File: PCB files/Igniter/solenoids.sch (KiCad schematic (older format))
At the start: 28 parts, among them Q2 N MOSFET, Q3 N MOSFET, Q4 N MOSFET, Q5 N MOSFET, Q6 N MOSFET, U2 FDS8984, U3 FDS8984, U4 FDS8984

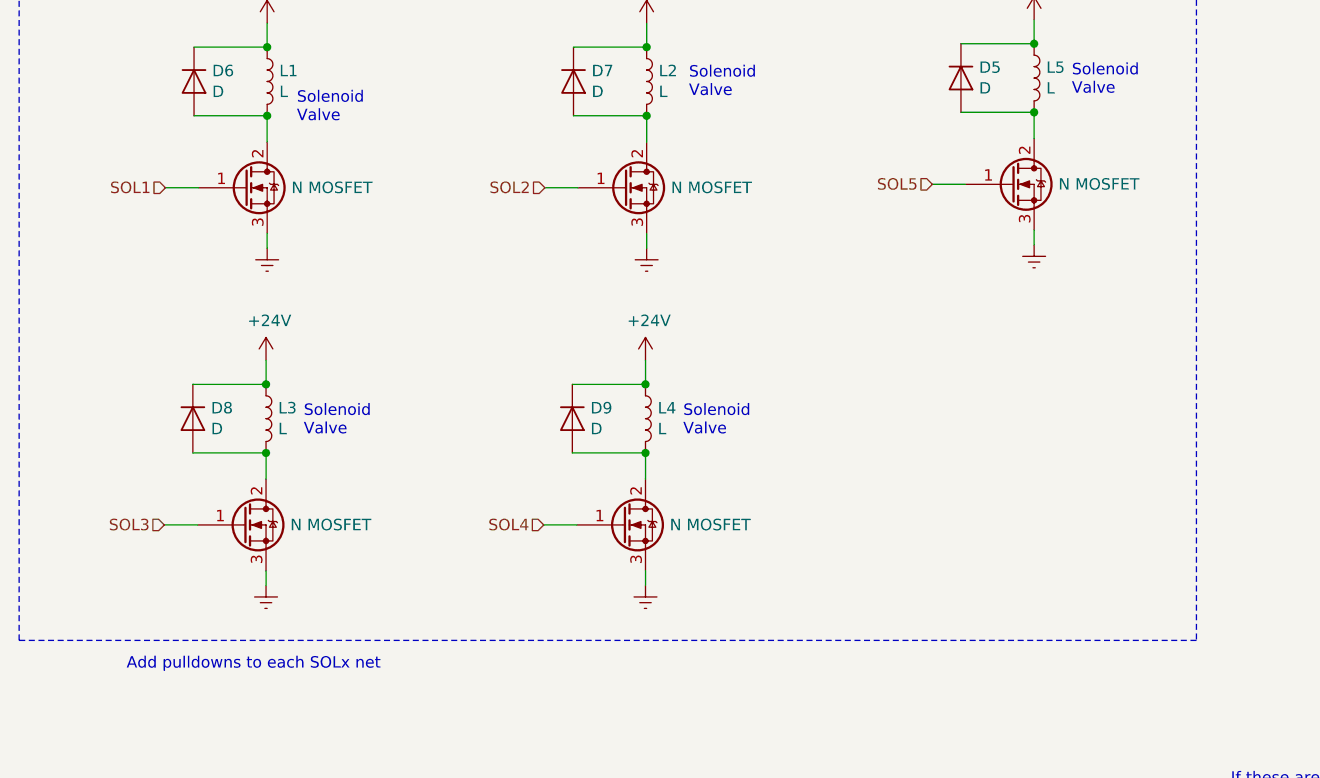
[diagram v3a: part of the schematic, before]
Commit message: 11/16/2019
-Selected smaller MOSFET SOT223
-Condensed PCB to a much smaller size
-Added Solenoid pulldowns
-Added all momentary switches
-Shrunk all resistors to 1206
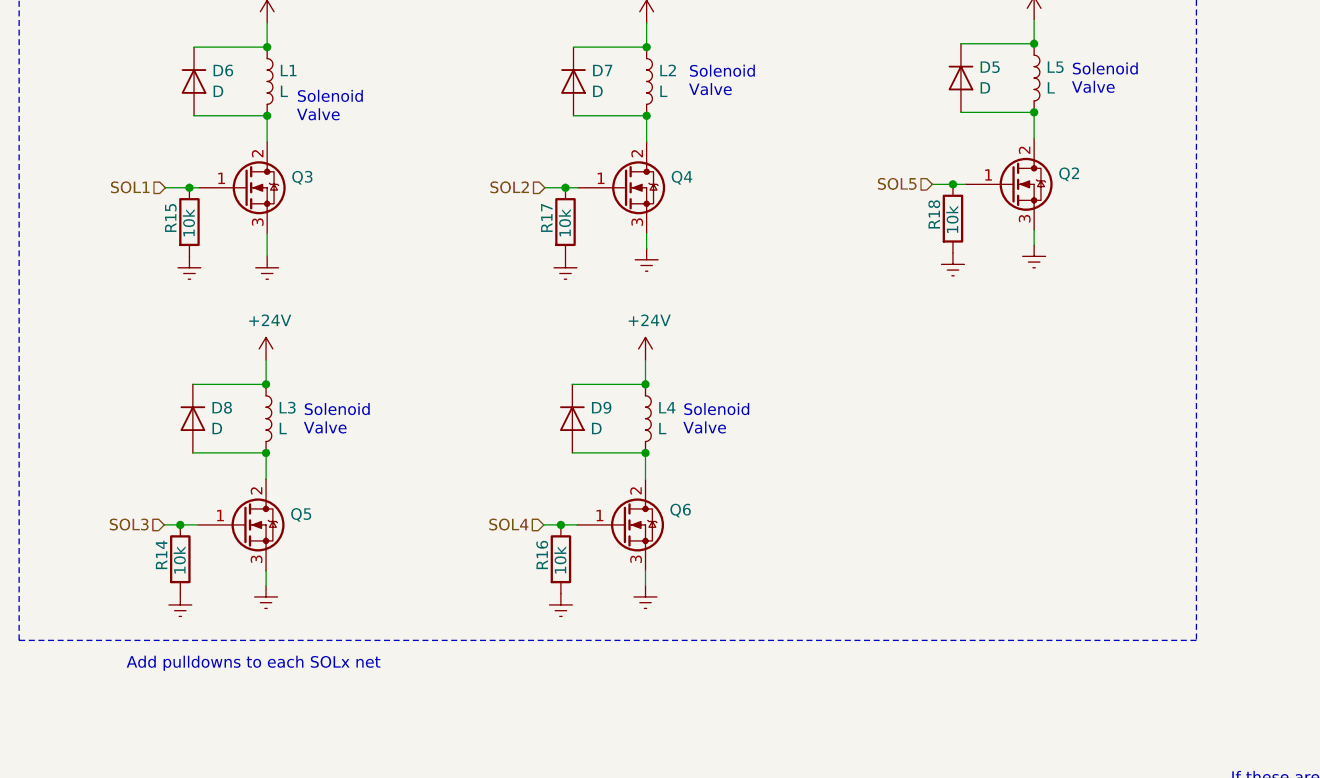
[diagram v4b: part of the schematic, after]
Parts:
- added R14, R15, R16, R17, R18: 10k, Resistor_SMD:R_1206_3216Metric, symbol Device:R
- Q2, Q3, Q4, Q5, Q6: footprint Package_TO_SOT_SMD:TO-263-3_TabPin2 -> Package_TO_SOT_SMD:SOT-223
- R10, R5, R7, R8, R9: footprint Resistor_SMD:R_1210_3225Metric -> Resistor_SMD:R_1206_3216Metric
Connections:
- net GNDREF: now also R14.2, R15.2, R16.2, R17.2, R18.2
- net SOL1: now also R15.1
- net SOL2: now also R17.1
- net SOL3: now also R14.1
- net SOL4: now also R16.1
- net SOL5: now also R18.1
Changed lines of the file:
@@
 	1830 2635 2150 2635
 Connection ~ 2150 2335
-Wire Wire Line
-	1705 2950 1850 2950
 Text Notes 2280 2670 0    50   ~ 0
 Solenoid\nValve
@@
 L power:GNDREF #PWR029
 U 1 1 5DB4DF2B
-P 2150 3215
-F 0 "#PWR029" H 2150 2965 50  0001 C CNN
-F 1 "GNDREF" H 2155 3042 50  0001 C CNN
-F 2 "" H 2150 3215 50  0001 C CNN
-F 3 "" H 2150 3215 50  0001 C CNN
-	1    2150 3215
-	1    0    0    -1
-$EndComp
-Wire Wire Line
-	2150 3150 2150 3215
+P 2150 3250
+F 0 "#PWR029" H 2150 3000 50  0001 C CNN
+F 1 "GNDREF" H 2155 3077 50  0001 C CNN
+F 2 "" H 2150 3250 50  0001 C CNN
+F 3 "" H 2150 3250 50  0001 C CNN
+	1    2150 3250
+	1    0    0    -1
+$EndComp
+Wire Wire Line
+	2150 3150 2150 3250
 $Comp
 L Device:Q_NMOS_GDS Q?
@@
 AR Path="/5DB4DFB4" Ref="Q?"  Part="1"
 AR Path="/5DB4D508/5DB4DFB4" Ref="Q3"  Part="1"
-F 0 "Q3" H 2256 2996 50  0001 L CNN
-F 1 "N MOSFET" H 2256 2950 50  0000 L CNN
-F 2 "Package_TO_SOT_SMD:TO-263-3_TabPin2" H 2250 3050 50  0001 C CNN
+F 0 "Q3" H 2256 2996 50  0000 L CNN
+F 1 "N MOSFET" H 2256 2950 50  0001 L CNN
+F 2 "Package_TO_SOT_SMD:SOT-223" H 2250 3050 50  0001 C CNN
 F 3 "~" H 2050 2950 50  0001 C CNN
 	1    2050 2950
@@
 AR Path="/5DB4DFC6" Ref="Q?"  Part="1"
 AR Path="/5DB4D508/5DB4DFC6" Ref="Q5"  Part="1"
-F 0 "Q5" H 2251 4471 50  0001 L CNN
-F 1 "N MOSFET" H 2251 4425 50  0000 L CNN
-F 2 "Package_TO_SOT_SMD:TO-263-3_TabPin2" H 2245 4525 50  0001 C CNN
+F 0 "Q5" H 2251 4471 50  0000 L CNN
+F 1 "N MOSFET" H 2251 4425 50  0001 L CNN
+F 2 "Package_TO_SOT_SMD:SOT-223" H 2245 4525 50  0001 C CNN
 F 3 "~" H 2045 4425 50  0001 C CNN
 	1    2045 4425
@@
 AR Path="/5DB4DFC0" Ref="Q?"  Part="1"
 AR Path="/5DB4D508/5DB4DFC0" Ref="Q6"  Part="1"
-F 0 "Q6" H 3911 4471 50  0001 L CNN
-F 1 "N MOSFET" H 3911 4425 50  0000 L CNN
-F 2 "Package_TO_SOT_SMD:TO-263-3_TabPin2" H 3905 4525 50  0001 C CNN
+F 0 "Q6" H 3910 4490 50  0000 L CNN
+F 1 "N MOSFET" H 3911 4425 50  0001 L CNN
+F 2 "Package_TO_SOT_SMD:SOT-223" H 3905 4525 50  0001 C CNN
 F 3 "~" H 3705 4425 50  0001 C CNN
 	1    3705 4425
@@
 Solenoid\nValve
 Wire Wire Line
-	3360 4425 3505 4425
+	3360 4425 3435 4425
 Wire Wire Line
 	3485 4110 3805 4110
@@
 Solenoid\nValve
 Wire Wire Line
-	1700 4425 1845 4425
+	1700 4425 1770 4425
 Wire Wire Line
 	1825 4110 2145 4110
@@
 AR Path="/5DB4DFF7" Ref="Q?"  Part="1"
 AR Path="/5DB4D508/5DB4DFF7" Ref="Q2"  Part="1"
-F 0 "Q2" H 5611 2981 50  0001 L CNN
-F 1 "N MOSFET" H 5611 2935 50  0000 L CNN
-F 2 "Package_TO_SOT_SMD:TO-263-3_TabPin2" H 5605 3035 50  0001 C CNN
+F 0 "Q2" H 5611 2981 50  0000 L CNN
+F 1 "N MOSFET" H 5611 2935 50  0001 L CNN
+F 2 "Package_TO_SOT_SMD:SOT-223" H 5605 3035 50  0001 C CNN
 F 3 "~" H 5405 2935 50  0001 C CNN
 	1    5405 2935
@@
 Solenoid\nValve
 Wire Wire Line
-	5060 2935 5205 2935
+	5060 2935 5150 2935
 Wire Wire Line
 	5185 2620 5505 2620
@@
 AR Path="/5DB4DFBA" Ref="Q?"  Part="1"
 AR Path="/5DB4D508/5DB4DFBA" Ref="Q4"  Part="1"
-F 0 "Q4" H 3916 2996 50  0001 L CNN
-F 1 "N MOSFET" H 3916 2950 50  0000 L CNN
-F 2 "Package_TO_SOT_SMD:TO-263-3_TabPin2" H 3910 3050 50  0001 C CNN
+F 0 "Q4" H 3916 2996 50  0000 L CNN
+F 1 "N MOSFET" H 3916 2950 50  0001 L CNN
+F 2 "Package_TO_SOT_SMD:SOT-223" H 3910 3050 50  0001 C CNN
 F 3 "~" H 3710 2950 50  0001 C CNN
 	1    3710 2950
@@
 	3810 2230 3810 2335
 Wire Wire Line
-	3365 2950 3510 2950
+	3365 2950 3455 2950
 Wire Wire Line
 	3490 2635 3810 2635
@@
 F 0 "R5" V 7155 2890 50  0000 C CNN
 F 1 "1k2" V 7235 2890 50  0000 C CNN
-F 2 "Resistor_SMD:R_1210_3225Metric" V 7165 2890 50  0001 C CNN
+F 2 "Resistor_SMD:R_1206_3216Metric" V 7165 2890 50  0001 C CNN
 F 3 "~" H 7235 2890 50  0001 C CNN
 	1    7235 2890
@@
 F 0 "R8" V 7390 3090 50  0000 C CNN
 F 1 "1k2" V 7475 3090 50  0000 C CNN
-F 2 "Resistor_SMD:R_1210_3225Metric" V 7405 3090 50  0001 C CNN
+F 2 "Resistor_SMD:R_1206_3216Metric" V 7405 3090 50  0001 C CNN
 F 3 "~" H 7475 3090 50  0001 C CNN
 	1    7475 3090
@@
 F 0 "R10" V 8885 3110 50  0000 C CNN
 F 1 "1k2" V 8965 3110 50  0000 C CNN
-F 2 "Resistor_SMD:R_1210_3225Metric" V 8895 3110 50  0001 C CNN
+F 2 "Resistor_SMD:R_1206_3216Metric" V 8895 3110 50  0001 C CNN
 F 3 "~" H 8965 3110 50  0001 C CNN
 	1    8965 3110
@@
 F 0 "R7" V 7155 3760 50  0000 C CNN
 F 1 "1k2" V 7235 3760 50  0000 C CNN
-F 2 "Resistor_SMD:R_1210_3225Metric" V 7165 3760 50  0001 C CNN
+F 2 "Resistor_SMD:R_1206_3216Metric" V 7165 3760 50  0001 C CNN
 F 3 "~" H 7235 3760 50  0001 C CNN
 	1    7235 3760
@@
 F 0 "R9" V 7395 3960 50  0000 C CNN
 F 1 "1k2" V 7475 3960 50  0000 C CNN
-F 2 "Resistor_SMD:R_1210_3225Metric" V 7405 3960 50  0001 C CNN
+F 2 "Resistor_SMD:R_1206_3216Metric" V 7405 3960 50  0001 C CNN
 F 3 "~" H 7475 3960 50  0001 C CNN
 	1    7475 3960
@@
 Text Notes 1535 5065 0    50   ~ 0
 Add pulldowns to each SOLx net
+$Comp
+L Device:R R?
+U 1 1 5DD0DFB3
+P 1810 3100
+AR Path="/5DD0DFB3" Ref="R?"  Part="1"
+AR Path="/5DB4D508/5DD0DFB3" Ref="R15"  Part="1"
+F 0 "R15" V 1730 3050 50  0000 L CNN
+F 1 "10k" V 1810 3030 50  0000 L CNN
+F 2 "Resistor_SMD:R_1206_3216Metric" V 1740 3100 50  0001 C CNN
+F 3 "~" H 1810 3100 50  0001 C CNN
+	1    1810 3100
+	1    0    0    -1
+$EndComp
+$Comp
+L power:GNDREF #PWR?
+U 1 1 5DD0DFBA
+P 1810 3250
+AR Path="/5DD0DFBA" Ref="#PWR?"  Part="1"
+AR Path="/5DB4D508/5DD0DFBA" Ref="#PWR050"  Part="1"
+F 0 "#PWR050" H 1810 3000 50  0001 C CNN
+F 1 "GNDREF" H 1815 3077 50  0001 C CNN
+F 2 "" H 1810 3250 50  0001 C CNN
+F 3 "" H 1810 3250 50  0001 C CNN
+	1    1810 3250
+	1    0    0    -1
+$EndComp
+Wire Wire Line
+	1850 2950 1810 2950
+Wire Wire Line
+	1810 2950 1705 2950
+Connection ~ 1810 2950
+$Comp
+L Device:R R?
+U 1 1 5DD11B80
+P 3455 3100
+AR Path="/5DD11B80" Ref="R?"  Part="1"
+AR Path="/5DB4D508/5DD11B80" Ref="R17"  Part="1"
+F 0 "R17" V 3375 3050 50  0000 L CNN
+F 1 "10k" V 3455 3030 50  0000 L CNN
+F 2 "Resistor_SMD:R_1206_3216Metric" V 3385 3100 50  0001 C CNN
+F 3 "~" H 3455 3100 50  0001 C CNN
+	1    3455 3100
+	1    0    0    -1
+$EndComp
+$Comp
+L power:GNDREF #PWR?
+U 1 1 5DD11B86
+P 3455 3250
+AR Path="/5DD11B86" Ref="#PWR?"  Part="1"
+AR Path="/5DB4D508/5DD11B86" Ref="#PWR052"  Part="1"
+F 0 "#PWR052" H 3455 3000 50  0001 C CNN
+F 1 "GNDREF" H 3460 3077 50  0001 C CNN
+F 2 "" H 3455 3250 50  0001 C CNN
+F 3 "" H 3455 3250 50  0001 C CNN
+	1    3455 3250
+	1    0    0    -1
+$EndComp
+Connection ~ 3455 2950
+Wire Wire Line
+	3455 2950 3510 2950
+$Comp
+L Device:R R?
+U 1 1 5DD1276B
+P 5150 3085
+AR Path="/5DD1276B" Ref="R?"  Part="1"
+AR Path="/5DB4D508/5DD1276B" Ref="R18"  Part="1"
+F 0 "R18" V 5070 3035 50  0000 L CNN
+F 1 "10k" V 5150 3015 50  0000 L CNN
+F 2 "Resistor_SMD:R_1206_3216Metric" V 5080 3085 50  0001 C CNN
+F 3 "~" H 5150 3085 50  0001 C CNN
+	1    5150 3085
+	1    0    0    -1
+$EndComp
+$Comp
+L power:GNDREF #PWR?
+U 1 1 5DD12771
+P 5150 3235
+AR Path="/5DD12771" Ref="#PWR?"  Part="1"
+AR Path="/5DB4D508/5DD12771" Ref="#PWR053"  Part="1"
+F 0 "#PWR053" H 5150 2985 50  0001 C CNN
+F 1 "GNDREF" H 5155 3062 50  0001 C CNN
+F 2 "" H 5150 3235 50  0001 C CNN
+F 3 "" H 5150 3235 50  0001 C CNN
+	1    5150 3235
+	1    0    0    -1
+$EndComp
+Connection ~ 5150 2935
+Wire Wire Line
+	5150 2935 5205 2935
+$Comp
+L Device:R R?
+U 1 1 5DD1351F
+P 1770 4575
+AR Path="/5DD1351F" Ref="R?"  Part="1"
+AR Path="/5DB4D508/5DD1351F" Ref="R14"  Part="1"
+F 0 "R14" V 1690 4525 50  0000 L CNN
+F 1 "10k" V 1770 4505 50  0000 L CNN
+F 2 "Resistor_SMD:R_1206_3216Metric" V 1700 4575 50  0001 C CNN
+F 3 "~" H 1770 4575 50  0001 C CNN
+	1    1770 4575
+	1    0    0    -1
+$EndComp
+$Comp
+L power:GNDREF #PWR?
+U 1 1 5DD13525
+P 1770 4725
+AR Path="/5DD13525" Ref="#PWR?"  Part="1"
+AR Path="/5DB4D508/5DD13525" Ref="#PWR049"  Part="1"
+F 0 "#PWR049" H 1770 4475 50  0001 C CNN
+F 1 "GNDREF" H 1775 4552 50  0001 C CNN
+F 2 "" H 1770 4725 50  0001 C CNN
+F 3 "" H 1770 4725 50  0001 C CNN
+	1    1770 4725
+	1    0    0    -1
+$EndComp
+Connection ~ 1770 4425
+Wire Wire Line
+	1770 4425 1845 4425
+$Comp
+L Device:R R?
+U 1 1 5DD14222
+P 3435 4575
+AR Path="/5DD14222" Ref="R?"  Part="1"
+AR Path="/5DB4D508/5DD14222" Ref="R16"  Part="1"
+F 0 "R16" V 3355 4525 50  0000 L CNN
+F 1 "10k" V 3435 4505 50  0000 L CNN
+F 2 "Resistor_SMD:R_1206_3216Metric" V 3365 4575 50  0001 C CNN
+F 3 "~" H 3435 4575 50  0001 C CNN
+	1    3435 4575
+	1    0    0    -1
+$EndComp
+$Comp
+L power:GNDREF #PWR?
+U 1 1 5DD14228
+P 3435 4725
+AR Path="/5DD14228" Ref="#PWR?"  Part="1"
+AR Path="/5DB4D508/5DD14228" Ref="#PWR051"  Part="1"
+F 0 "#PWR051" H 3435 4475 50  0001 C CNN
+F 1 "GNDREF" H 3440 4552 50  0001 C CNN
+F 2 "" H 3435 4725 50  0001 C CNN
+F 3 "" H 3435 4725 50  0001 C CNN
+	1    3435 4725
+	1    0    0    -1
+$EndComp
+Connection ~ 3435 4425
+Wire Wire Line
+	3435 4425 3505 4425
 $EndSCHEMATC

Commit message: 11/16/2019
-Changed references to group footprints on the board
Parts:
- renumbered D12 to D10, D13 to D11, D6 to D2, D7 to D3, D5 to D4, D8 to D5, D9 to D6, D4 to D7, D11 to D8, D10 to D9, Q3 to Q2, Q4 to Q3, Q2 to Q4
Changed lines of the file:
@@
 $EndComp
 $Comp
-L Device:D D6
+L Device:D D2
 U 1 1 5DB4DF0F
 P 1830 2485
-F 0 "D6" V 1784 2564 50  0000 L CNN
+F 0 "D2" V 1784 2564 50  0000 L CNN
 F 1 "D" V 1875 2564 50  0000 L CNN
 F 2 "Diode_SMD:D_SOD-123F" H 1830 2485 50  0001 C CNN
@@
 AR Path="/5D9BEB88/5DB4DFB4" Ref="Q?"  Part="1"
 AR Path="/5DB4DFB4" Ref="Q?"  Part="1"
-AR Path="/5DB4D508/5DB4DFB4" Ref="Q3"  Part="1"
-F 0 "Q3" H 2256 2996 50  0000 L CNN
+AR Path="/5DB4D508/5DB4DFB4" Ref="Q2"  Part="1"
+F 0 "Q2" H 2256 2996 50  0000 L CNN
 F 1 "N MOSFET" H 2256 2950 50  0001 L CNN
 F 2 "Package_TO_SOT_SMD:SOT-223" H 2250 3050 50  0001 C CNN
@@
 	3805 3810 3485 3810
 $Comp
-L Device:D D9
+L Device:D D6
 U 1 1 5DB4DF8F
 P 3485 3960
-F 0 "D9" V 3439 4039 50  0000 L CNN
+F 0 "D6" V 3439 4039 50  0000 L CNN
 F 1 "D" V 3530 4039 50  0000 L CNN
 F 2 "Diode_SMD:D_SOD-123F" H 3485 3960 50  0001 C CNN
@@
 	2145 3810 1825 3810
 $Comp
-L Device:D D8
+L Device:D D5
 U 1 1 5DB4DF3A
 P 1825 3960
-F 0 "D8" V 1779 4039 50  0000 L CNN
+F 0 "D5" V 1779 4039 50  0000 L CNN
 F 1 "D" V 1870 4039 50  0000 L CNN
 F 2 "Diode_SMD:D_SOD-123F" H 1825 3960 50  0001 C CNN
@@
 AR Path="/5D9BEB88/5DB4DFF7" Ref="Q?"  Part="1"
 AR Path="/5DB4DFF7" Ref="Q?"  Part="1"
-AR Path="/5DB4D508/5DB4DFF7" Ref="Q2"  Part="1"
-F 0 "Q2" H 5611 2981 50  0000 L CNN
+AR Path="/5DB4D508/5DB4DFF7" Ref="Q4"  Part="1"
+F 0 "Q4" H 5611 2981 50  0000 L CNN
 F 1 "N MOSFET" H 5611 2935 50  0001 L CNN
 F 2 "Package_TO_SOT_SMD:SOT-223" H 5605 3035 50  0001 C CNN
@@
 	5505 2320 5185 2320
 $Comp
-L Device:D D5
+L Device:D D4
 U 1 1 5DB4DFD3
 P 5185 2470
-F 0 "D5" V 5139 2549 50  0000 L CNN
+F 0 "D4" V 5139 2549 50  0000 L CNN
 F 1 "D" V 5230 2549 50  0000 L CNN
 F 2 "Diode_SMD:D_SOD-123F" H 5185 2470 50  0001 C CNN
@@
 AR Path="/5D9BEB88/5DB4DFBA" Ref="Q?"  Part="1"
 AR Path="/5DB4DFBA" Ref="Q?"  Part="1"
-AR Path="/5DB4D508/5DB4DFBA" Ref="Q4"  Part="1"
-F 0 "Q4" H 3916 2996 50  0000 L CNN
+AR Path="/5DB4D508/5DB4DFBA" Ref="Q3"  Part="1"
+F 0 "Q3" H 3916 2996 50  0000 L CNN
 F 1 "N MOSFET" H 3916 2950 50  0001 L CNN
 F 2 "Package_TO_SOT_SMD:SOT-223" H 3910 3050 50  0001 C CNN
@@
 	3810 2335 3490 2335
 $Comp
-L Device:D D7
+L Device:D D3
 U 1 1 5DB4DF65
 P 3490 2485
-F 0 "D7" V 3444 2564 50  0000 L CNN
+F 0 "D3" V 3444 2564 50  0000 L CNN
 F 1 "D" V 3535 2564 50  0000 L CNN
 F 2 "Diode_SMD:D_SOD-123F" H 3490 2485 50  0001 C CNN
@@
 $EndBitmap
 $Comp
-L Device:LED D4
+L Device:LED D7
 U 1 1 5DD6B6EC
 P 7045 3265
-AR Path="/5DB4D508/5DD6B6EC" Ref="D4"  Part="1"
+AR Path="/5DB4D508/5DD6B6EC" Ref="D7"  Part="1"
 AR Path="/5DD6B6EC" Ref="D?"  Part="1"
-F 0 "D4" H 7045 3180 50  0000 C CNN
+F 0 "D7" H 7045 3180 50  0000 C CNN
 F 1 "LED" H 7045 3365 50  0000 C CNN
 F 2 "LED_SMD:LED_1206_3216Metric" H 7045 3265 50  0001 C CNN
@@
 SOL2
 $Comp
-L Device:LED D11
+L Device:LED D8
 U 1 1 5DD6B701
 P 7320 3265
-AR Path="/5DB4D508/5DD6B701" Ref="D11"  Part="1"
+AR Path="/5DB4D508/5DD6B701" Ref="D8"  Part="1"
 AR Path="/5DD6B701" Ref="D?"  Part="1"
-F 0 "D11" H 7320 3180 50  0000 C CNN
+F 0 "D8" H 7320 3180 50  0000 C CNN
 F 1 "LED" H 7320 3365 50  0000 C CNN
 F 2 "LED_SMD:LED_1206_3216Metric" H 7320 3265 50  0001 C CNN
@@
 Connection ~ 8225 2790
 $Comp
-L Device:LED D13
+L Device:LED D11
 U 1 1 5DD6B726
 P 8815 3295
-AR Path="/5DB4D508/5DD6B726" Ref="D13"  Part="1"
+AR Path="/5DB4D508/5DD6B726" Ref="D11"  Part="1"
 AR Path="/5DD6B726" Ref="D?"  Part="1"
-F 0 "D13" H 8815 3210 50  0000 C CNN
+F 0 "D11" H 8815 3210 50  0000 C CNN
 F 1 "LED" H 8815 3395 50  0000 C CNN
 F 2 "LED_SMD:LED_1206_3216Metric" H 8815 3295 50  0001 C CNN
@@
 	7045 2890 7085 2890
 $Comp
-L Device:LED D10
+L Device:LED D9
 U 1 1 5DD6B752
 P 7045 4135
-AR Path="/5DB4D508/5DD6B752" Ref="D10"  Part="1"
+AR Path="/5DB4D508/5DD6B752" Ref="D9"  Part="1"
 AR Path="/5DD6B752" Ref="D?"  Part="1"
-F 0 "D10" H 7045 4050 50  0000 C CNN
+F 0 "D9" H 7045 4050 50  0000 C CNN
 F 1 "LED" H 7045 4235 50  0000 C CNN
 F 2 "LED_SMD:LED_1206_3216Metric" H 7045 4135 50  0001 C CNN
@@
 $EndComp
 $Comp
-L Device:LED D12
+L Device:LED D10
 U 1 1 5DD6B764
 P 7320 4135
-AR Path="/5DB4D508/5DD6B764" Ref="D12"  Part="1"
+AR Path="/5DB4D508/5DD6B764" Ref="D10"  Part="1"
 AR Path="/5DD6B764" Ref="D?"  Part="1"
-F 0 "D12" H 7320 4050 50  0000 C CNN
+F 0 "D10" H 7320 4050 50  0000 C CNN
 F 1 "LED" H 7320 4235 50  0000 C CNN
 F 2 "LED_SMD:LED_1206_3216Metric" H 7320 4135 50  0001 C CNN
